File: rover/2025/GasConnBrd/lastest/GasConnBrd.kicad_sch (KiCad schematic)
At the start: 7 parts

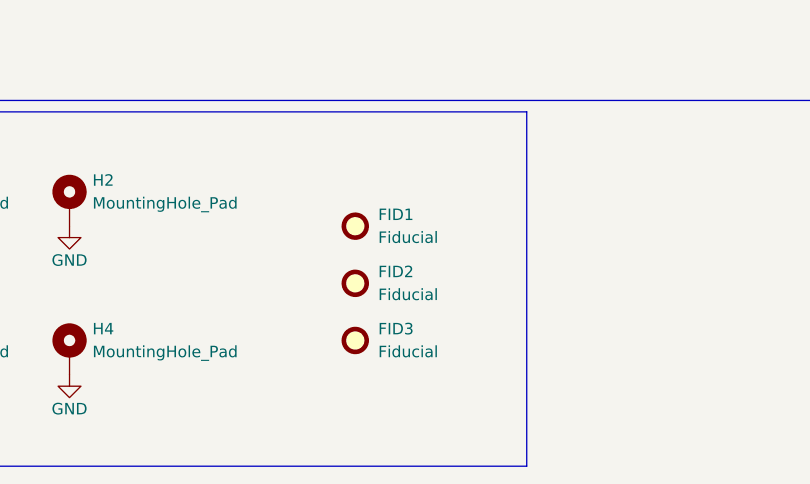
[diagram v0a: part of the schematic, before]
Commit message: Creat project folder from template
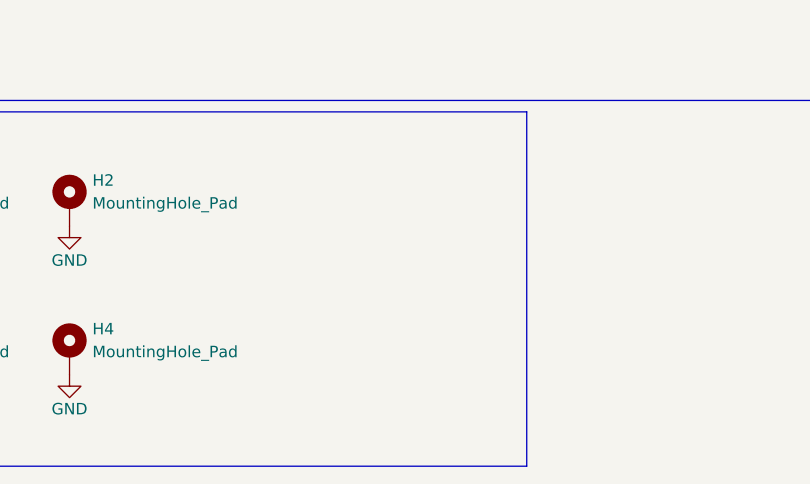
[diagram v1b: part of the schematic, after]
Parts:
- removed FID1, FID2, FID3: Fiducial, symbol Mechanical:Fiducial
- H1, H2, H3, H4: footprint MountingHole:MountingHole_3.2mm_M3_DIN965_Pad_TopBottom -> RoverFootprints:MountingHole
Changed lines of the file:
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@@
 			)
 		)
-		(property "Footprint" "MountingHole:MountingHole_3.2mm_M3_DIN965_Pad_TopBottom"
+		(property "Footprint" "RoverFootprints:MountingHole"
 			(at 57.15 121.92 0)
 			(effects
@@
 			)
 		)
-		(property "Footprint" "MountingHole:MountingHole_3.2mm_M3_DIN965_Pad_TopBottom"
+		(property "Footprint" "RoverFootprints:MountingHole"
 			(at 57.15 105.41 0)
 			(effects
@@
 			)
 		)
-		(property "Footprint" "MountingHole:MountingHole_3.2mm_M3_DIN965_Pad_TopBottom"
+		(property "Footprint" "RoverFootprints:MountingHole"
 			(at 82.55 105.41 0)
 			(effects
@@
 			)
 		)
-		(property "Footprint" "MountingHole:MountingHole_3.2mm_M3_DIN965_Pad_TopBottom"
+		(property "Footprint" "RoverFootprints:MountingHole"
 			(at 82.55 121.92 0)
 			(effects
@@
 	)
 	(symbol
-		(lib_id "Mechanical:Fiducial")
-		(at 114.3 120.65 0)
-		(unit 1)
-		(exclude_from_sim yes)
-		(in_bom no)
-		(on_board yes)
-		(dnp no)
-		(fields_autoplaced yes)
-		(property "Reference" "FID3"
-			(at 116.84 119.3799 0)
-			(effects
-				(font
-					(size 1.27 1.27)
-				)
-				(justify left)
-			)
-		)
-		(property "Value" "Fiducial"
-			(at 116.84 121.9199 0)
-			(effects
-				(font
-					(size 1.27 1.27)
-				)
-				(justify left)
-			)
-		)
-		(property "Footprint" ""
-			(at 114.3 120.65 0)
-			(effects
-				(font
-					(size 1.27 1.27)
-				)
-				(hide yes)
-			)
-		)
-		(property "Datasheet" "~"
-			(at 114.3 120.65 0)
-			(effects
-				(font
-					(size 1.27 1.27)
-				)
-				(hide yes)
-			)
-		)
-		(property "Description" "Fiducial Marker"
-			(at 114.3 120.65 0)
-			(effects
-				(font
-					(size 1.27 1.27)
-				)
-				(hide yes)
-			)
-		)
-		(instances
-			(project "ProjectTemplate"
-				(path "/a4fa9b30-7b48-474a-bdaa-0d7a6d26a697"
-					(reference "FID3")
-					(unit 1)
-				)
-			)
-		)
-	)
-	(symbol
-		(lib_id "Mechanical:Fiducial")
-		(at 114.3 107.95 0)
-		(unit 1)
-		(exclude_from_sim yes)
-		(in_bom no)
-		(on_board yes)
-		(dnp no)
-		(fields_autoplaced yes)
-		(property "Reference" "FID1"
-			(at 116.84 106.6799 0)
-			(effects
-				(font
-					(size 1.27 1.27)
-				)
-				(justify left)
-			)
-		)
-		(property "Value" "Fiducial"
-			(at 116.84 109.2199 0)
-			(effects
-				(font
-					(size 1.27 1.27)
-				)
-				(justify left)
-			)
-		)
-		(property "Footprint" ""
-			(at 114.3 107.95 0)
-			(effects
-				(font
-					(size 1.27 1.27)
-				)
-				(hide yes)
-			)
-		)
-		(property "Datasheet" "~"
-			(at 114.3 107.95 0)
-			(effects
-				(font
-					(size 1.27 1.27)
-				)
-				(hide yes)
-			)
-		)
-		(property "Description" "Fiducial Marker"
-			(at 114.3 107.95 0)
-			(effects
-				(font
-					(size 1.27 1.27)
-				)
-				(hide yes)
-			)
-		)
-		(instances
-			(project ""
-				(path "/a4fa9b30-7b48-474a-bdaa-0d7a6d26a697"
-					(reference "FID1")
-					(unit 1)
-				)
-			)
-		)
-	)
-	(symbol
 		(lib_id "power:GND")
 		(at 57.15 124.46 0)
@@
 				(path "/a4fa9b30-7b48-474a-bdaa-0d7a6d26a697"
 					(reference "#PWR03")
-					(unit 1)
-				)
-			)
-		)
-	)
-	(symbol
-		(lib_id "Mechanical:Fiducial")
-		(at 114.3 114.3 0)
-		(unit 1)
-		(exclude_from_sim yes)
-		(in_bom no)
-		(on_board yes)
-		(dnp no)
-		(fields_autoplaced yes)
-		(property "Reference" "FID2"
-			(at 116.84 113.0299 0)
-			(effects
-				(font
-					(size 1.27 1.27)
-				)
-				(justify left)
-			)
-		)
-		(property "Value" "Fiducial"
-			(at 116.84 115.5699 0)
-			(effects
-				(font
-					(size 1.27 1.27)
-				)
-				(justify left)
-			)
-		)
-		(property "Footprint" ""
-			(at 114.3 114.3 0)
-			(effects
-				(font
-					(size 1.27 1.27)
-				)
-				(hide yes)
-			)
-		)
-		(property "Datasheet" "~"
-			(at 114.3 114.3 0)
-			(effects
-				(font
-					(size 1.27 1.27)
-				)
-				(hide yes)
-			)
-		)
-		(property "Description" "Fiducial Marker"
-			(at 114.3 114.3 0)
-			(effects
-				(font
-					(size 1.27 1.27)
-				)
-				(hide yes)
-			)
-		)
-		(instances
-			(project "ProjectTemplate"
-				(path "/a4fa9b30-7b48-474a-bdaa-0d7a6d26a697"
-					(reference "FID2")
 					(unit 1)
 				)
@@
 		)
 		(instances
-			(project "ProjectTemplate"
+			(project "GasConnBrd"
 				(path "/a4fa9b30-7b48-474a-bdaa-0d7a6d26a697"
 					(page "2")

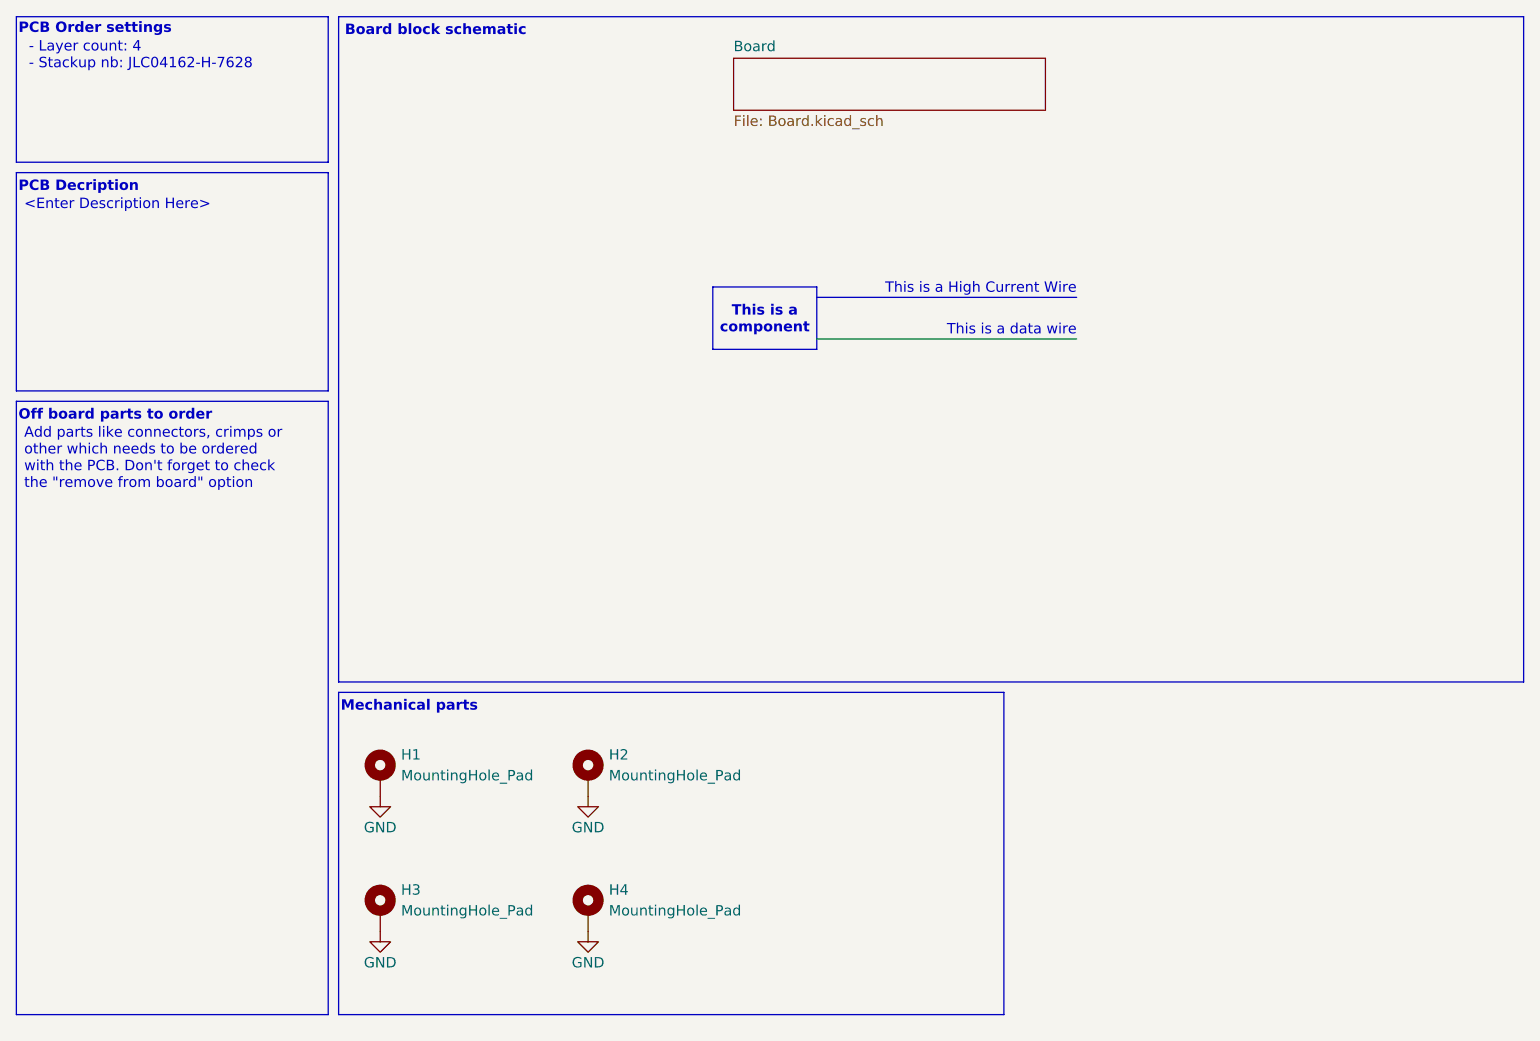
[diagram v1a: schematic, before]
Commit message: Esp+Pwr_Added
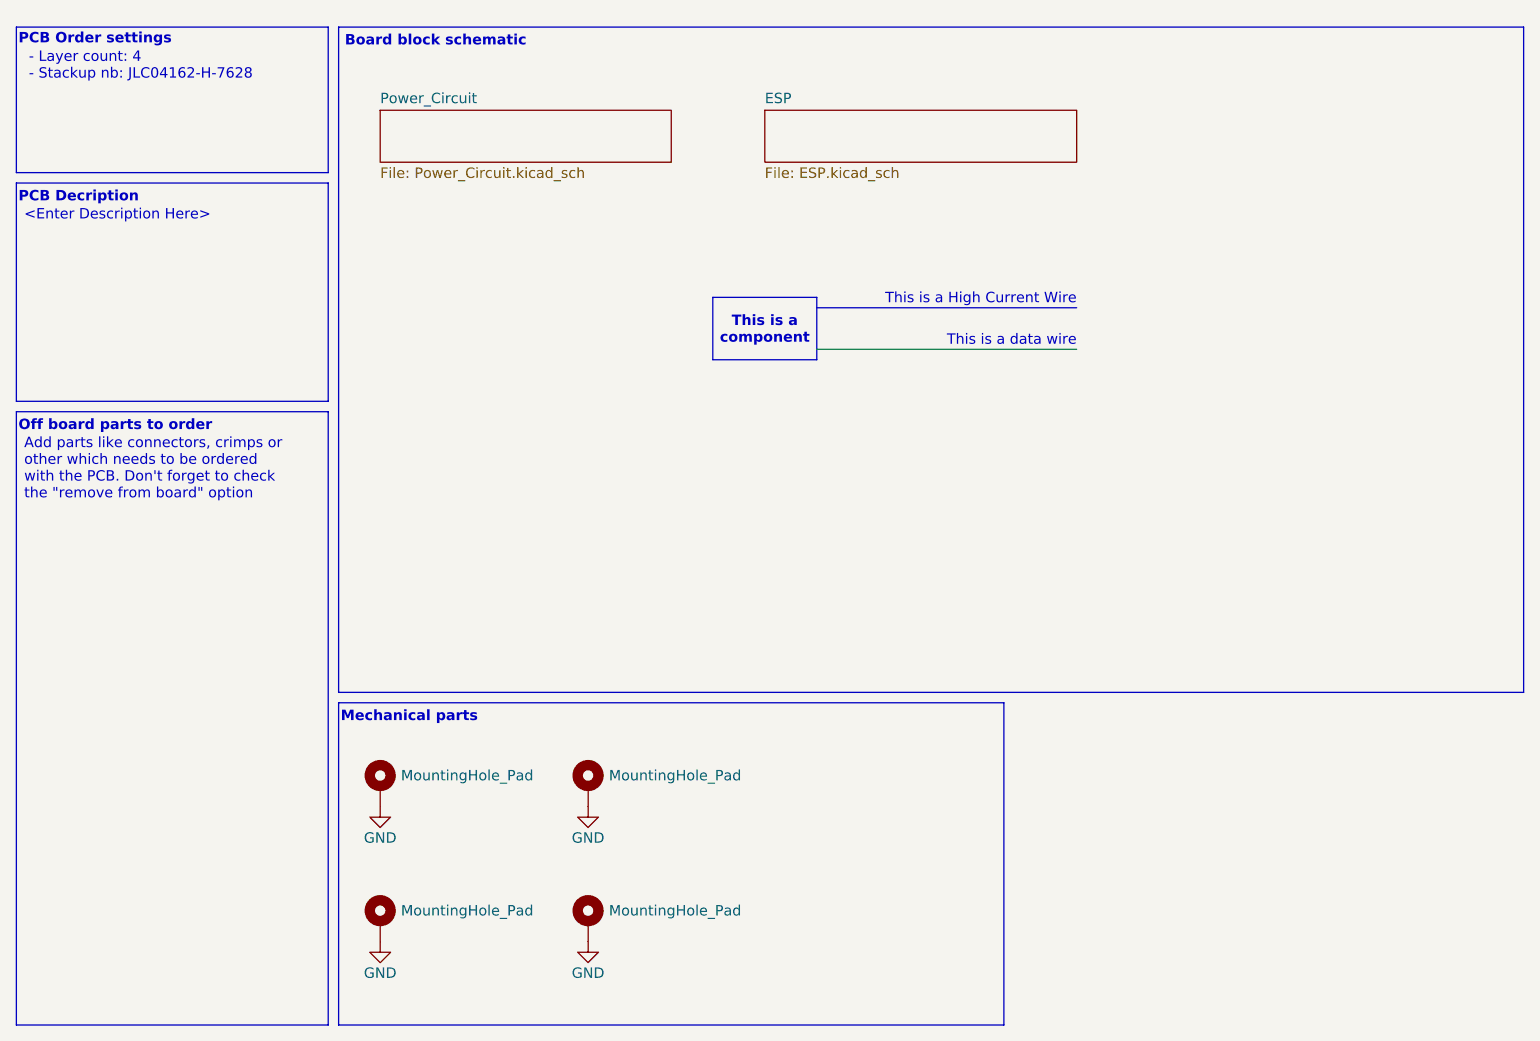
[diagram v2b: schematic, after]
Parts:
- removed H1, H2, H3, H4: MountingHole_Pad, RoverFootprints:MountingHole, symbol RoverLibrary:MountingHole_Pad
- added H10, H11, H12, H9: MountingHole_Pad, RoverFootprint:MountingHole, symbol RoverLibrary:MountingHole_Pad
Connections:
- net GND: now also H10.1, H11.1, H12.1, H9.1
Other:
- removed sheet Board
- added sheet ESP (ESP.kicad_sch)
- added sheet Power_Circuit (Power_Circuit.kicad_sch)

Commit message: PCB finit
A faire approuver au besoin
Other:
- added sheet Extras (Extras.kicad_sch)
- added sheet Sensors (Sensors.kicad_sch)
- note added: "Analog"
- note added: "I2C"
- note removed: "This is a High Current Wire"
- note removed: "This is a data wire"
